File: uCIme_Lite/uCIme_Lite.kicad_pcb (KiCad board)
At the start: 2 copper layers, 65 x 56 mm, 73 parts, among them J1 USB_MODE, J10 JACK_MODE, J11 SERIAL_MODE, J12 SERIAL_VOLTAGE_SELECT, J2 JACK_POWER_IN, J3 USB_POWER_IN, J4 USB_PC, J5 GPIO, J6 5V_ENABLE, J7 SERIAL, J8 JACK_POWER_OUT, J9 USB_POWER_OUT, Q1 BSS138, Q2 BUK7M27-80EX, Q3 BUK7M27-80EX, Q4 BSS138, Q5 BSS138, Q6 BSS138, Q7 BSS138, Q8 BSS138, U1 LM74502, U2 LM74502, U3 AP2204K-ADJ, U4 AP2204K-ADJ, U5 FT230XS, U6 TXB0104D

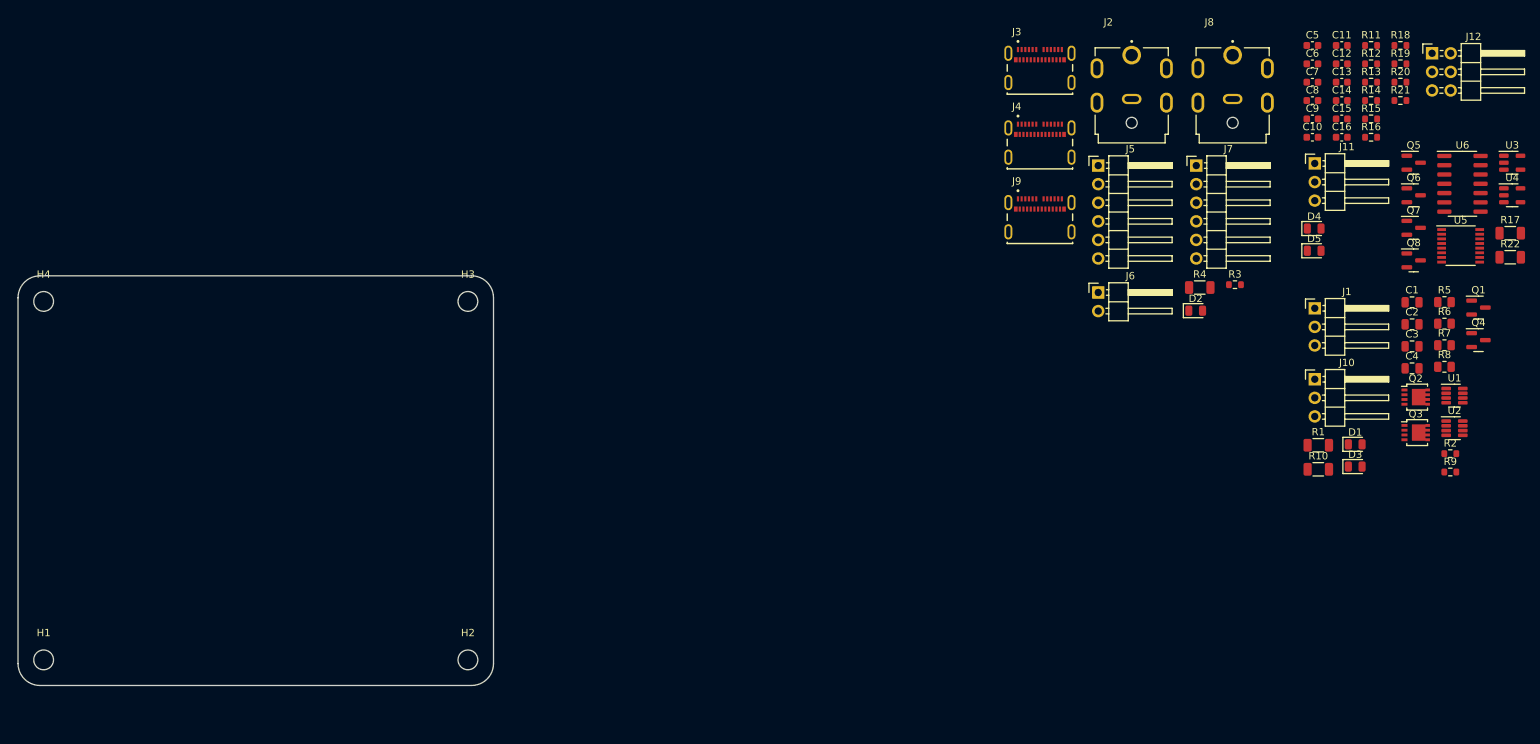
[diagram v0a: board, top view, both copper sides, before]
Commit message: lite: Configured PCB stackup and placed connectors.
Signed-off-by: Adrien Ricciardi <aricciardi@baylibre.com>
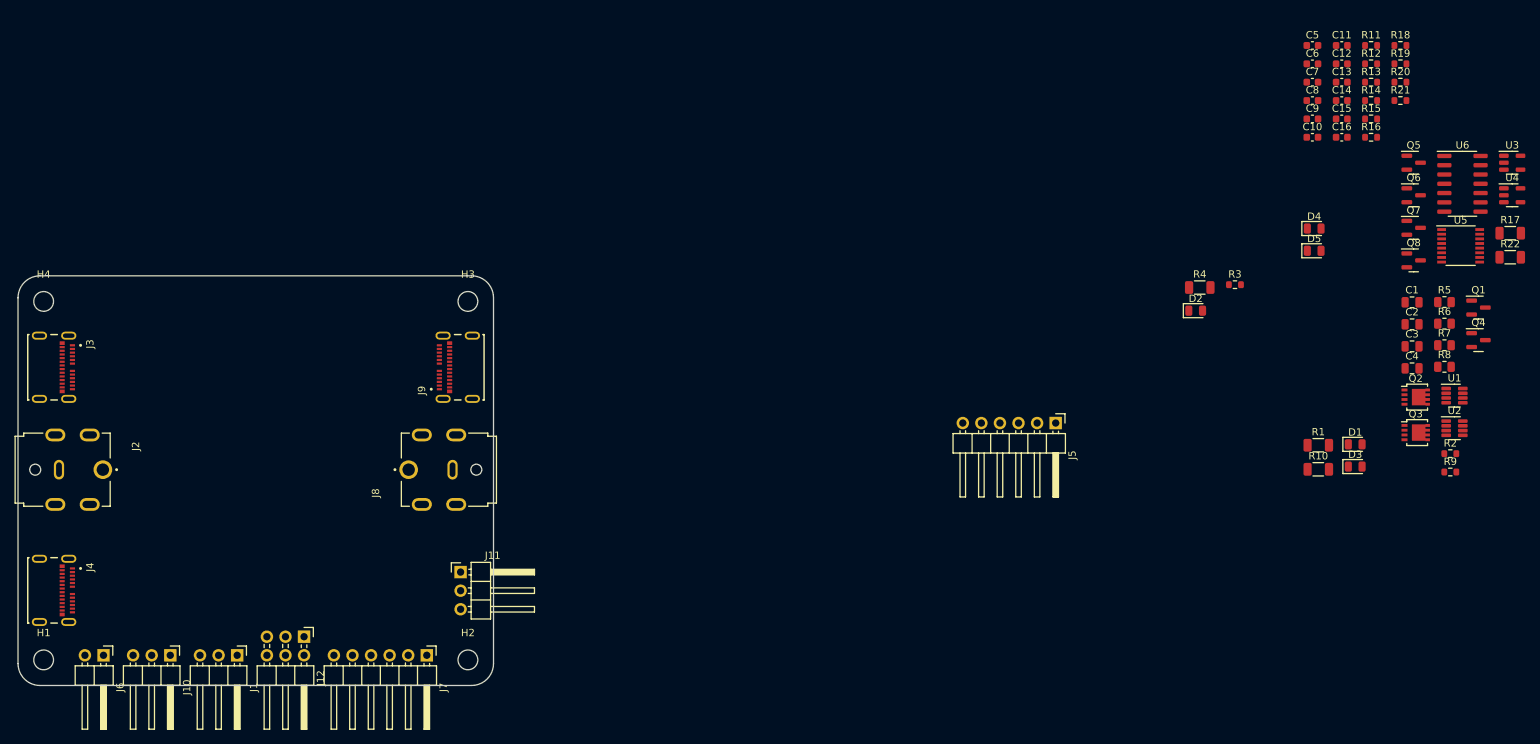
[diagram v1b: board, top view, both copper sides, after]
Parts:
- moved J12 173.6 mm to (104.1, 106.3), turned to -90 degrees
- moved J10 160.9 mm to (85.8, 108.9), turned to -90 degrees
- moved J1 154.8 mm to (95.0, 108.9), turned to -90 degrees
- moved J2 151.6 mm to (76.6, 83.5), turned to -90 degrees
- moved J4 148.7 mm to (68.5, 100.0), turned to -90 degrees
- moved J6 144.7 mm to (76.7, 108.9), turned to -90 degrees
- moved J3 141.8 mm to (68.5, 69.5), turned to -90 degrees
- moved J11 129.4 mm to (125.5, 97.5)
- moved J8 126.1 mm to (118.4, 83.5), turned to 90 degrees
- moved J7 124.7 mm to (120.9, 108.9), turned to -90 degrees
- moved J9 80.5 mm to (126.5, 69.5), turned to 90 degrees
- moved J5 35.7 mm to (206.8, 77.1), turned to -90 degrees
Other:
- copper layers 2 -> 4

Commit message: lite: Routed power USB-C High Speed and Super Speed differential pairs (without trace length matching for now).
Signed-off-by: Adrien Ricciardi <aricciardi@baylibre.com>
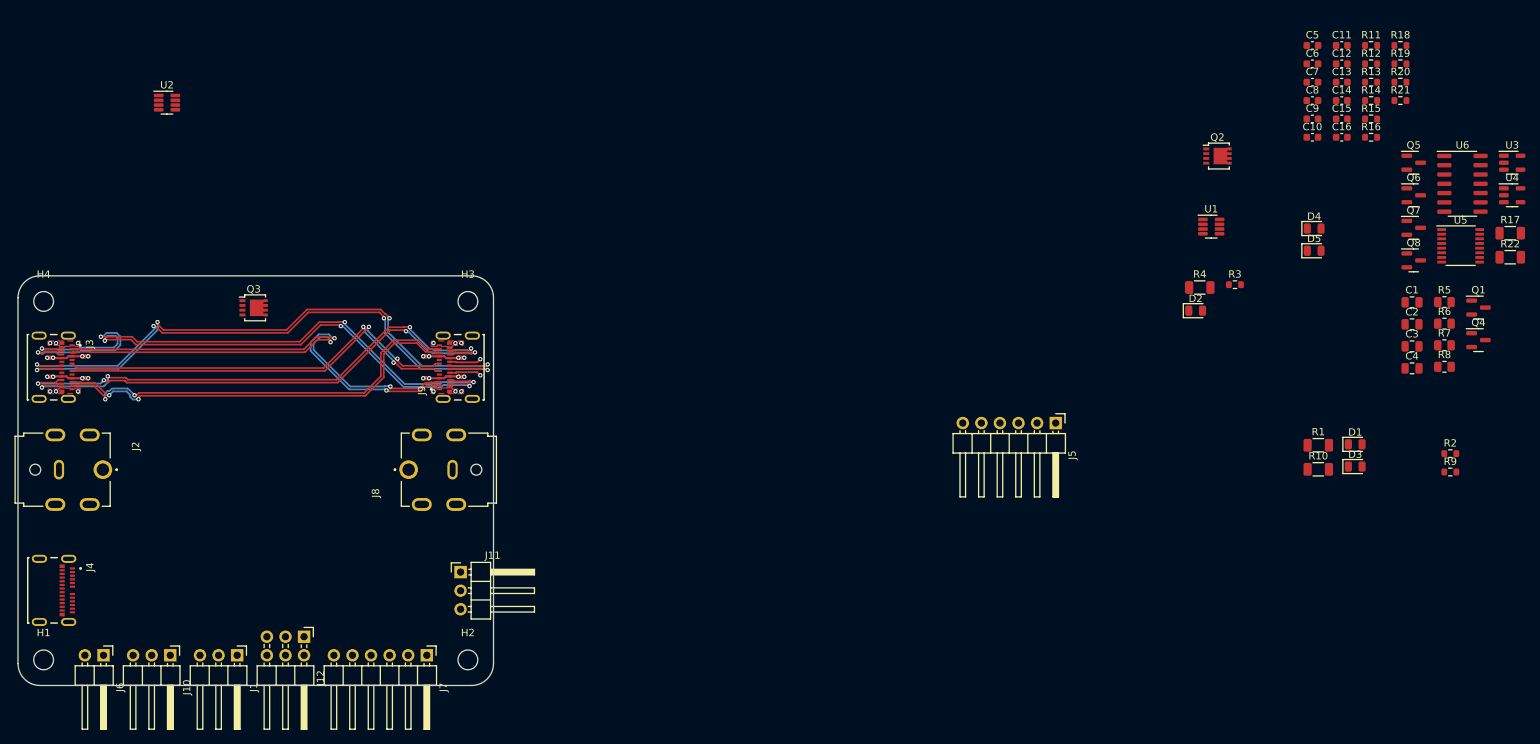
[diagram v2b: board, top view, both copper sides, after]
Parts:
- moved U2 181.5 mm to (85.4, 33.3)
- moved Q3 159.8 mm to (97.2, 61.4)
- moved Q2 42.7 mm to (229.0, 40.6)
- moved U1 40.5 mm to (228.1, 50.3)
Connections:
- C2 pad 1: +5V -> /Power Management/INPUT_USB_V+
- C4 pad 1: +5V -> /Power Management/INPUT_USB_V+
- J3 pad A4: +5V -> /Power Management/INPUT_USB_V+
- J3 pad A9: +5V -> /Power Management/INPUT_USB_V+
- J3 pad B4: +5V -> /Power Management/INPUT_USB_V+
- J3 pad B9: +5V -> /Power Management/INPUT_USB_V+
- J9 pad A4: +5V -> /Power Management/OUTPUT_USB_V+
- J9 pad A9: +5V -> /Power Management/OUTPUT_USB_V+
- J9 pad B4: +5V -> /Power Management/OUTPUT_USB_V+
- J9 pad B9: +5V -> /Power Management/OUTPUT_USB_V+
- Q3 pad 1: +5V -> /Power Management/OUTPUT_USB_V+
- Q3 pad 2: +5V -> /Power Management/OUTPUT_USB_V+
- Q3 pad 3: +5V -> /Power Management/OUTPUT_USB_V+
- Q3 pad 5: +5V -> /Power Management/INPUT_USB_V+
- R7 pad 1: +5V -> /Power Management/INPUT_USB_V+
- U2 pad 5: +5V -> /Power Management/INPUT_USB_V+
- U2 pad 8: +5V -> /Power Management/OUTPUT_USB_V+
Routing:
- net /D2_P: track 0.00 -> 80.2 mm, vias 0 -> 4
- net /SSRX1_N: track 0.00 -> 79.3 mm, vias 0 -> 4
- net /D2_N: track 0.00 -> 79.2 mm, vias 0 -> 4
- net /SSRX1_P: track 0.00 -> 75.0 mm, vias 0 -> 4
- net /SSTX2_N: track 0.00 -> 71.8 mm, vias 0 -> 4
- net /SSTX2_P: track 0.00 -> 71.3 mm, vias 0 -> 4
- net /SSTX1_P: track 0.00 -> 62.2 mm, vias 0 -> 2
- net /SSTX1_N: track 0.00 -> 60.3 mm, vias 0 -> 2
- net /SSRX2_P: track 0.00 -> 58.2 mm, vias 0 -> 2
- net /SSRX2_N: track 0.00 -> 57.6 mm, vias 0 -> 2
- net /D1_P: track 0.00 -> 55.9 mm, vias 0 -> 2
- net /D1_N: track 0.00 -> 55.8 mm, vias 0 -> 2
- net /Power Management/OUTPUT_USB_V+: track 0.00 -> 11.4 mm, vias 0 -> 8
- net /Power Management/INPUT_USB_V+: track 0.00 -> 11.4 mm, vias 0 -> 8
- net /SBU2: track 0.00 -> 4.41 mm, vias 0 -> 1
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- added copper zone on In2.Cu, net /Power Management/INPUT_USB_V+
- added copper zone on In2.Cu, net /Power Management/OUTPUT_USB_V+
- added copper zone on F.Cu, net GND
- added copper zone on In1.Cu, net GND

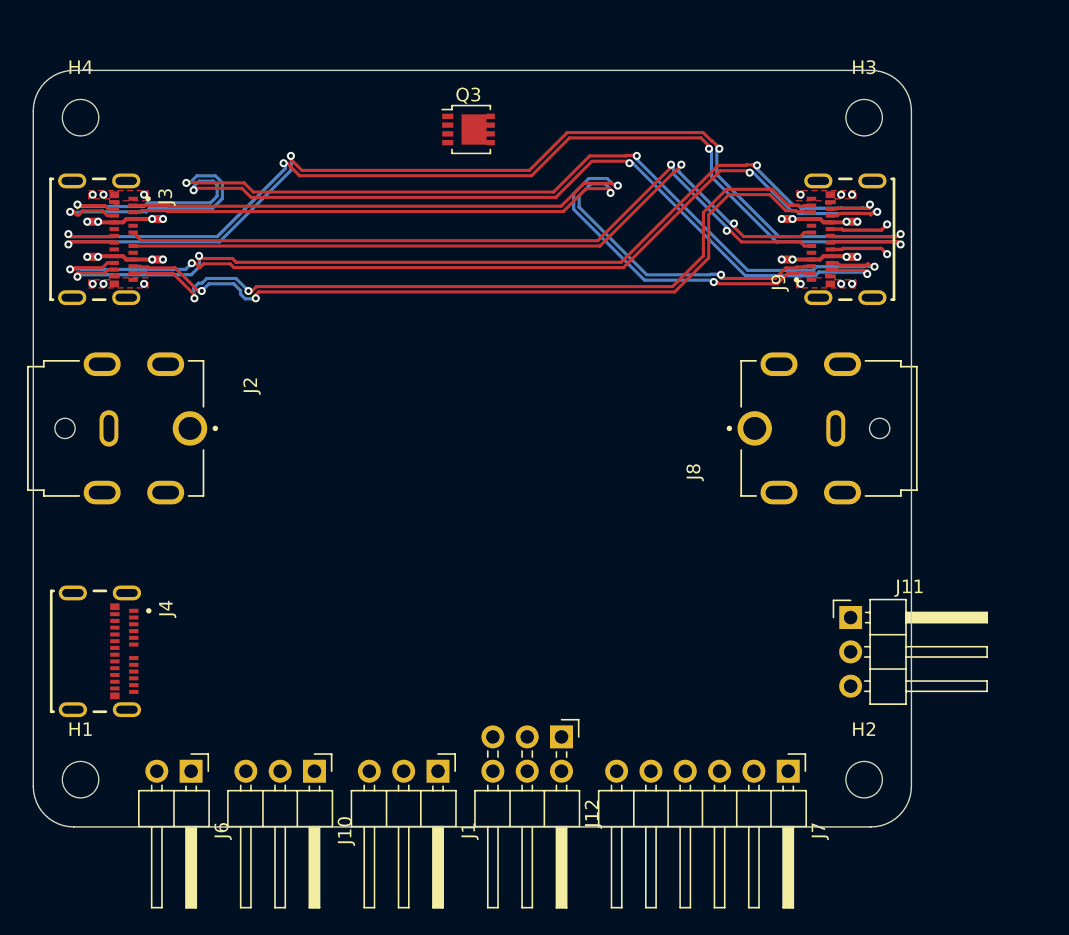
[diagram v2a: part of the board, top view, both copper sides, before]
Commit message: lite: Finished routing all power USB-C connectors signals.
Signed-off-by: Adrien Ricciardi <aricciardi@baylibre.com>
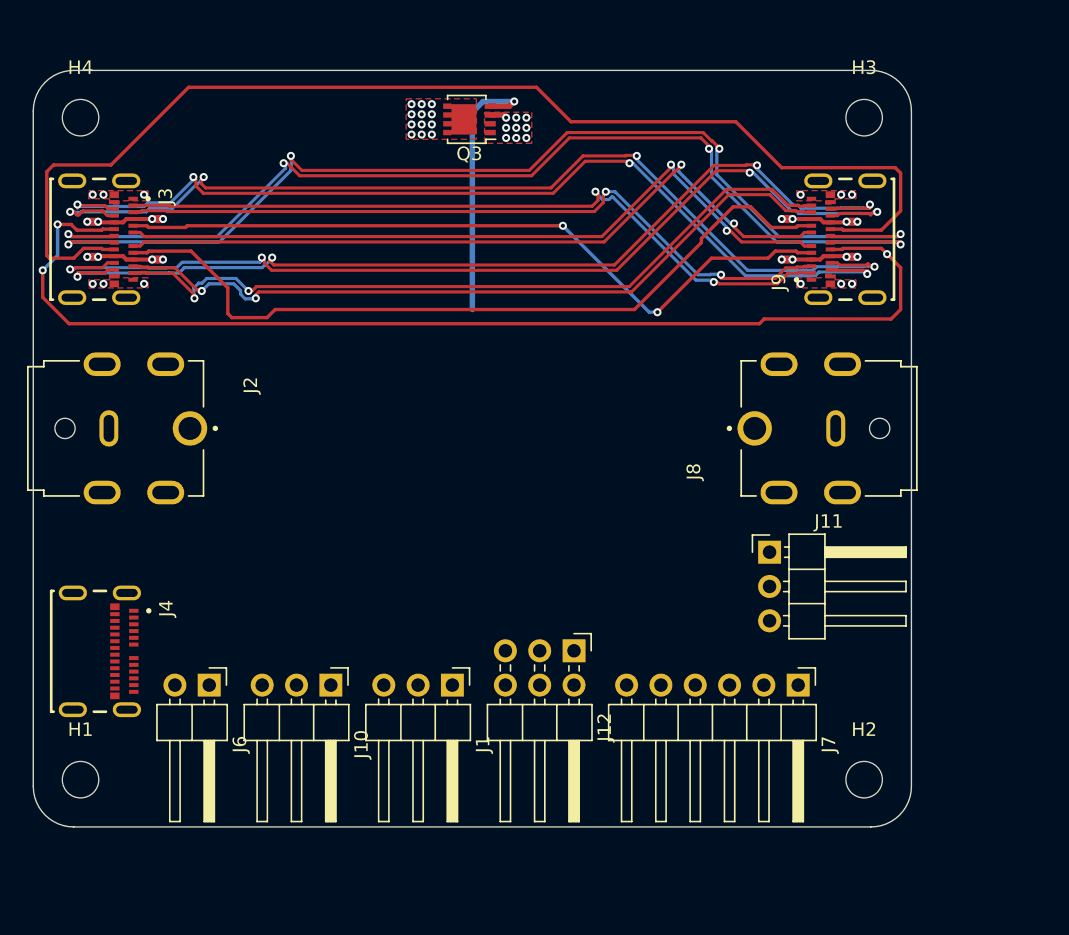
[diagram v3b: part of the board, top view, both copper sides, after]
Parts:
- moved J11 7.71 mm to (119.5, 92.7)
- moved J6 6.51 mm to (78.0, 102.5)
- moved J10 6.49 mm to (87.0, 102.5)
- moved J1 6.46 mm to (96.0, 102.5)
- moved J12 6.44 mm to (105.0, 100.0)
- moved J7 6.42 mm to (121.6, 102.5)
- moved Q3 0.75 mm to (97.3, 60.6), turned to 180 degrees
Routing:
- net /CC2: track 4.41 -> 88.6 mm, vias 1 -> 0
- net /SBU2: track 4.41 -> 83.9 mm, vias 1 -> 3
- net /SBU1: track 0.00 -> 57.7 mm
- net /CC1: track 0.00 -> 55.0 mm, vias 0 -> 2
- net Net-(Q3-G): track 0.00 -> 20.0 mm, vias 0 -> 1
- net /SSTX1_P: track 62.2 -> 54.7 mm
- net /SSTX1_N: track 60.3 -> 54.5 mm
- net /SSRX1_N: track 79.3 -> 73.5 mm
- net /SSRX1_P: track 75.0 -> 71.2 mm
- net /SSRX2_P: track 58.2 -> 56.3 mm
- net /SSRX2_N: track 57.6 -> 55.7 mm
- net /Power Management/OUTPUT_USB_V+: track 11.4 -> 12.7 mm, vias 8 -> 17
- net /SSTX2_N: track 71.8 -> 72.3 mm
- net /Power Management/INPUT_USB_V+: vias 8 -> 20
- added copper zone on F.Cu, net /Power Management/INPUT_USB_V+
- added copper zone on F.Cu, net /Power Management/OUTPUT_USB_V+

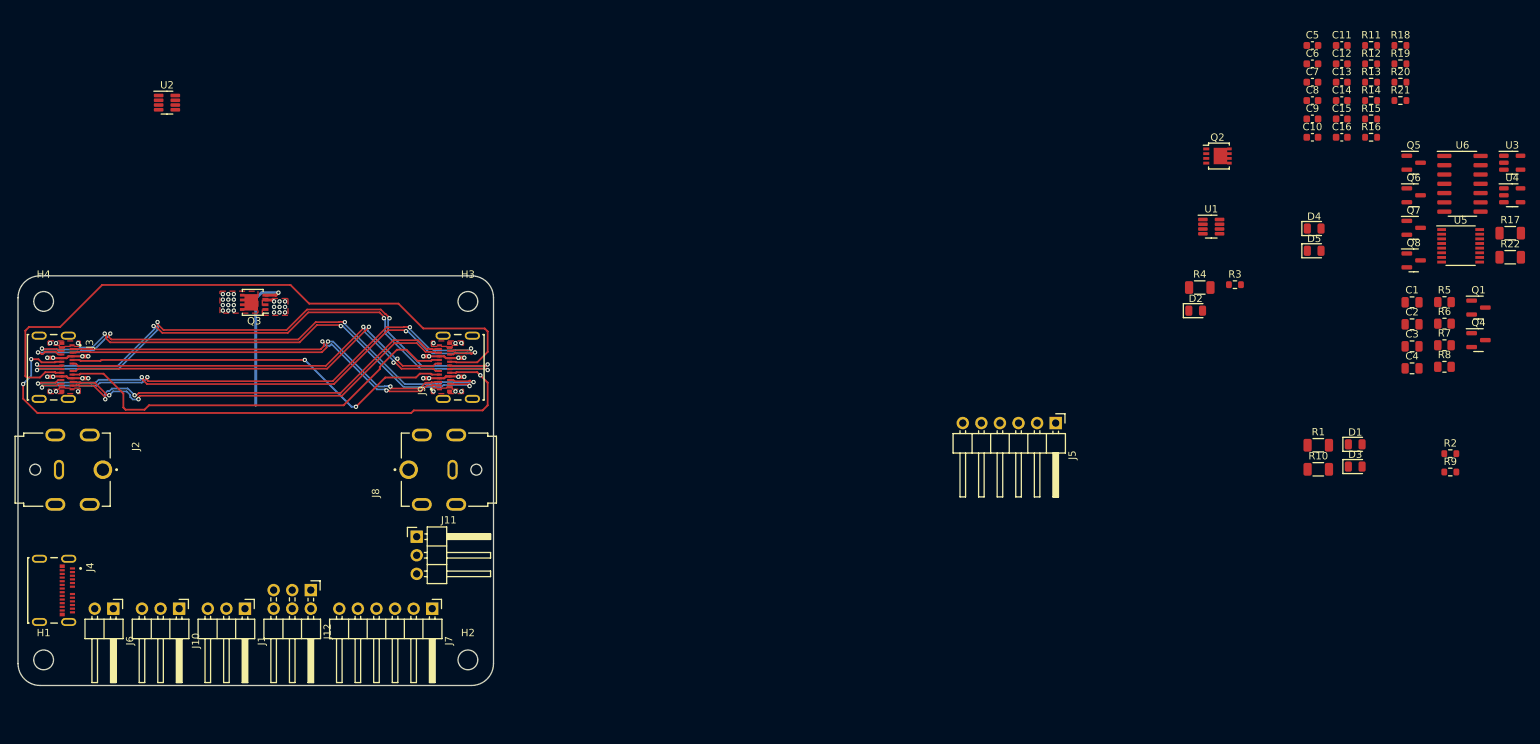
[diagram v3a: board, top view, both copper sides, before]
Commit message: lite: Routed power jack high-power traces.
Signed-off-by: Adrien Ricciardi <aricciardi@baylibre.com>
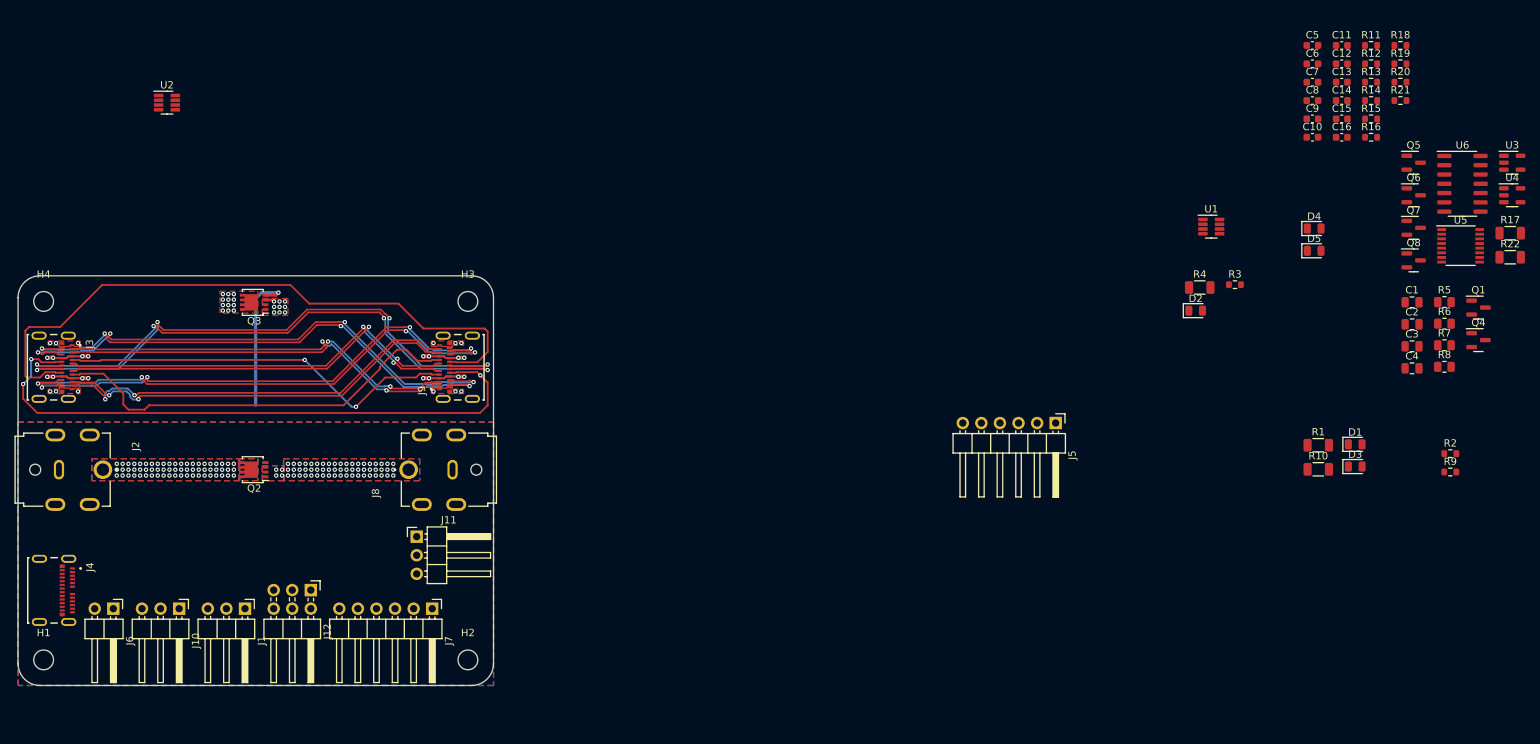
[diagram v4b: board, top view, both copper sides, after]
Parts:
- moved Q2 138.5 mm to (97.3, 83.5), turned to 180 degrees
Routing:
- net /Power Management/OUTPUT_JACK_V+: vias 0 -> 61
- net /Power Management/INPUT_JACK_V+: vias 0 -> 63
- added copper zone on B.Cu, net /Power Management/INPUT_JACK_V+
- added copper zone on F.Cu, net /Power Management/INPUT_JACK_V+
- added copper zone on In1.Cu, net /Power Management/INPUT_JACK_V+
- added copper zone on In2.Cu, net /Power Management/INPUT_JACK_V+
- added copper zone on B.Cu, net /Power Management/OUTPUT_JACK_V+
- added copper zone on F.Cu, net /Power Management/OUTPUT_JACK_V+
- added copper zone on In1.Cu, net /Power Management/OUTPUT_JACK_V+
- added copper zone on In2.Cu, net /Power Management/OUTPUT_JACK_V+
- added copper zone on B.Cu, net GND
- added copper zone on In2.Cu, net GND
